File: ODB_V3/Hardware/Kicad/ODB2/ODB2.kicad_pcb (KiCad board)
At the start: 4 copper layers, 63.5 x 127 mm, 238 parts, among them IC1 W25Q512JVEIQ, J1 1715310000, J10 GPS_Conn_02x04_Top_Bottom, J15 Vin_XT30PW-F, J2 RFD_GT17HN-4DP-2HA56, J3 SYS_SW_Conn_01x05_Header, J5 MEM2067, J6 IdeFIX_GT17HN-4DP-2HA56, J7 1715250000, J8 1715310000, J9 1715250000, U1 STM32F412ZGTx, U10 ADXL382-2BCCZ-RL7, U11 SI5442DU-T1-GE3, U12 SI5442DU-T1-GE3, U13 L6981N33DR, U2 LM339, U3 SI5442DU-T1-GE3, U4 MS580301BA01-00, U6 BNO055, U7 MPQ9843GLE-5-AEC1-Z, U8 SI5442DU-T1-GE3, U9 MAX6612MXK, Y1 ABM8G-25.000MHZ-18-D2Y-T

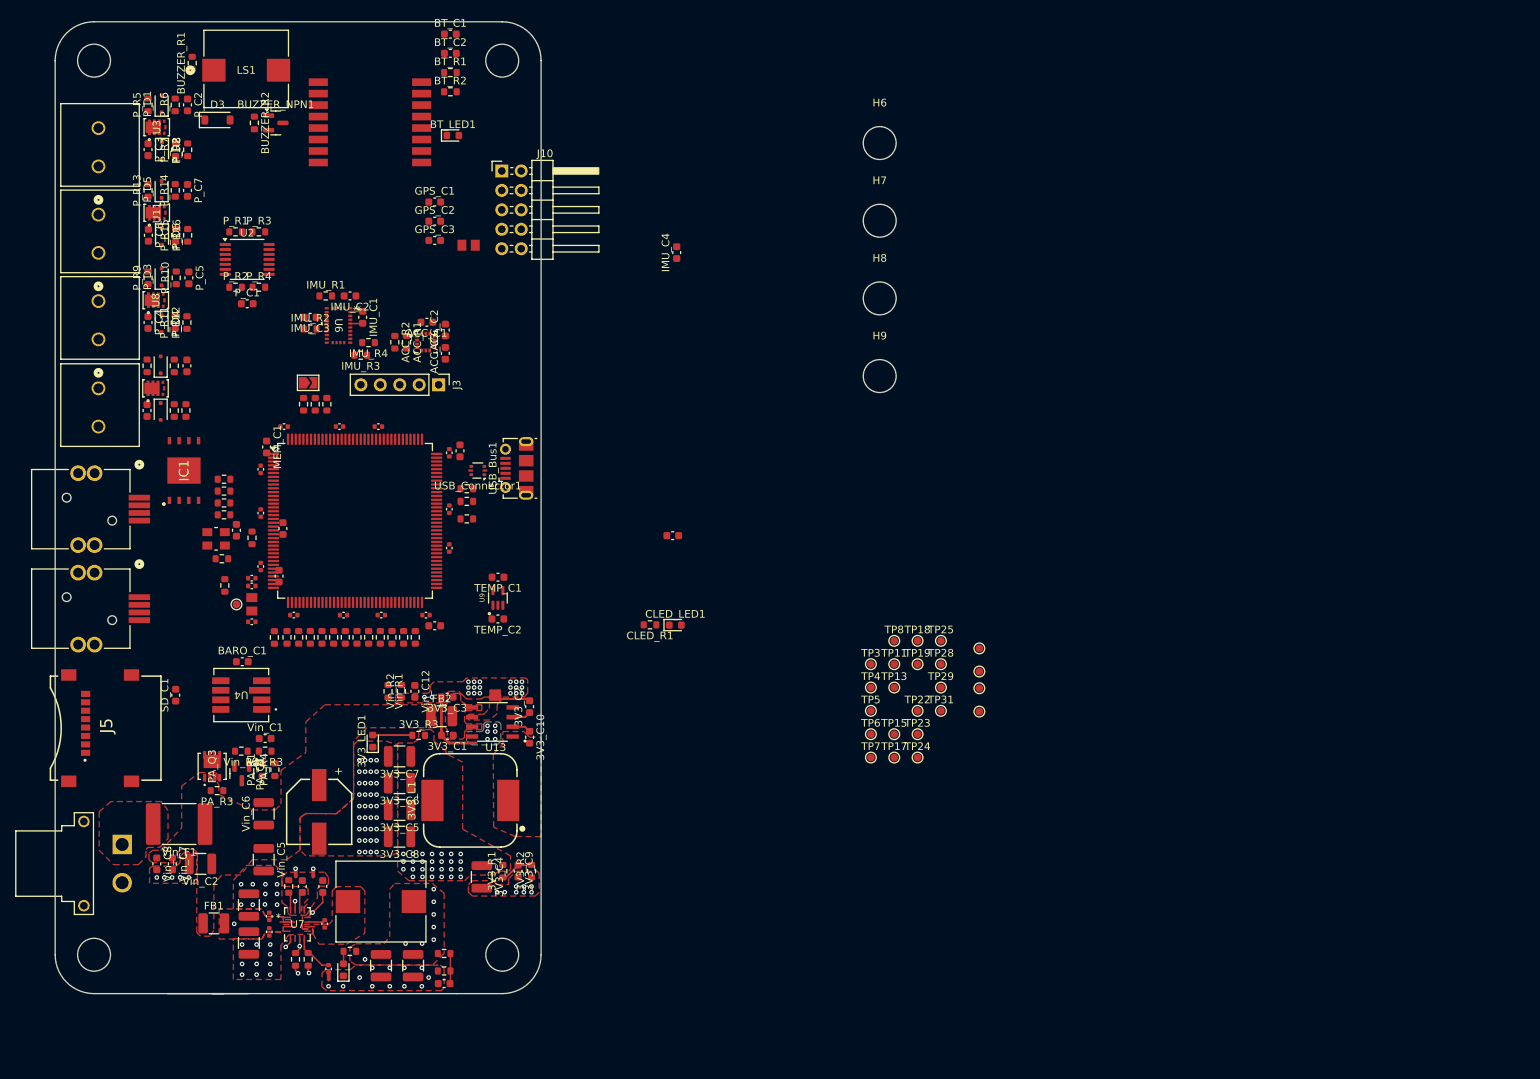
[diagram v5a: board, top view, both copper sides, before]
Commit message: WIP : finition layout, fix connecteur GPS, passage 4 couches -> 6 couches
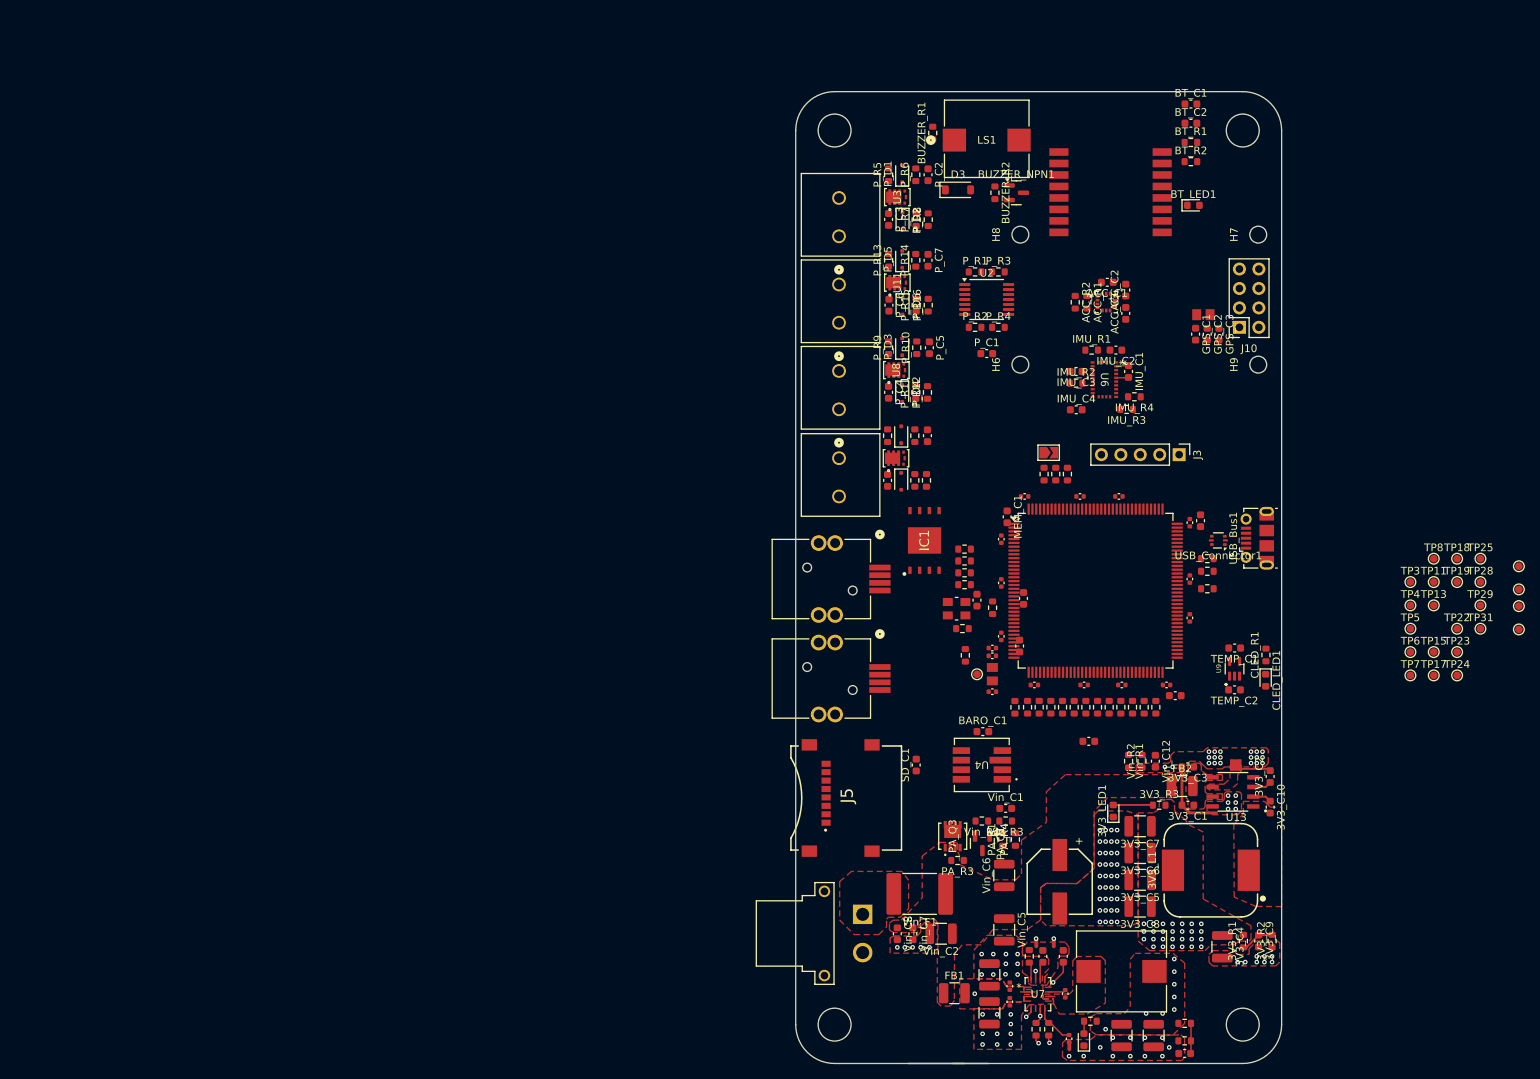
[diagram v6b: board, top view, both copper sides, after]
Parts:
- H6, H7, H8, H9: footprint MountingHole:MountingHole_4.3mm_M4 -> MountingHole:MountingHole_2.2mm_M2
- J10: footprint Connector_PinHeader_2.54mm:PinHeader_2x05_P2.54mm_Horizontal -> Connector_PinSocket_2.54mm:PinSocket_2x04_P2.54mm_Vertical
- moved GPS_C3 103.2 mm to (172.3, 60.8), turned to -90 degrees
- moved GPS_C2 102.0 mm to (170.8, 60.8), turned to -90 degrees
- moved GPS_C1 100.9 mm to (169.3, 60.8), turned to -90 degrees
- moved IMU_C1 100.3 mm to (160.5, 65.7)
- moved IMU_R1 100.3 mm to (155.7, 62.9)
- moved IMU_R4 100.3 mm to (161.3, 69.0)
- moved IMU_C3 100.3 mm to (153.7, 65.7)
- moved IMU_R2 100.3 mm to (153.7, 67.2)
- moved U6 100.3 mm to (157.4, 66.8)
- moved IMU_C2 100.3 mm to (158.9, 62.9)
- moved IMU_R3 100.3 mm to (160.3, 70.7)
- moved J10 98.5 mm to (175.0, 59.9), turned to 180 degrees
- moved Vin_C5 97.2 mm to (144.3, 138.7)
- moved 5V_C5 97.2 mm to (159.6, 152.5)
- moved BT_C1 97.2 mm to (168.7, 30.8)
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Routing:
- added copper zone on In3.Cu, net 5V_Main
- added copper zone on In4.Cu, net GND
- removed copper zone on In2.Cu, net 5V_Main
- removed copper zone on B.Cu, net GND
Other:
- copper layers 4 -> 6

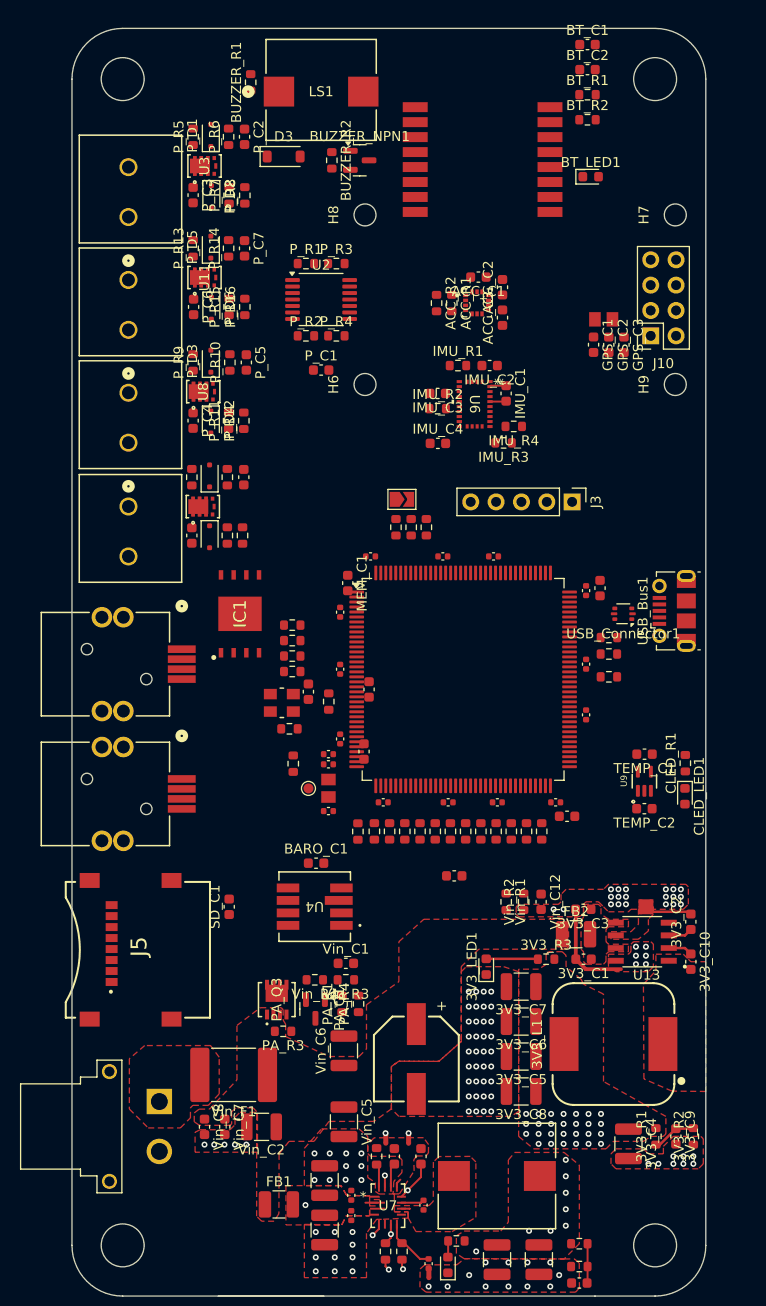
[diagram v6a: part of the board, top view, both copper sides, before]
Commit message: WIP : SD card under PCB, make board shorter in y axis
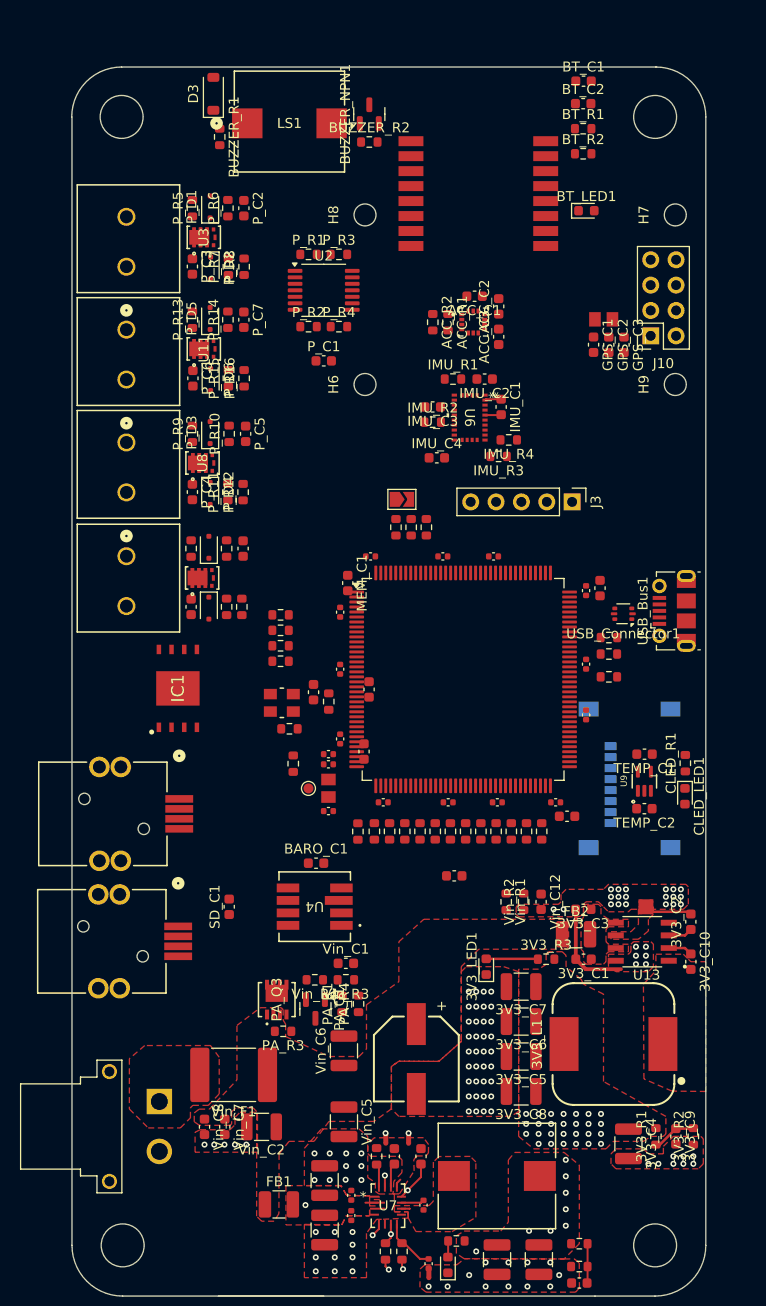
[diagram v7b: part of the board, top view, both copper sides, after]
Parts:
- J5: moved to B.Cu
- moved J5 52.9 mm to (173.6, 104.3), turned to 90 degrees
- moved J2 15.0 mm to (120.1, 107.8)
- moved J6 14.8 mm to (120.0, 120.6)
- moved IC1 9.72 mm to (127.6, 95.2)
- moved D3 9.43 mm to (131.2, 35.7), turned to 90 degrees
- moved P_D3 7.15 mm to (130.9, 69.6)
- moved P_D6 7.15 mm to (130.9, 64.3)
- moved P_C2 7.15 mm to (134.2, 47.1)
- moved P_C7 7.15 mm to (134.2, 58.3)
- moved P_C9 7.15 mm to (134.2, 81.2)
- moved P_D4 7.15 mm to (130.9, 75.7)
- moved P_D5 7.15 mm to (130.9, 58.2)
- moved P_D7 7.15 mm to (130.7, 81.1)
- moved P_D8 7.15 mm to (130.7, 87.2)
- moved P_R10 7.15 mm to (132.8, 69.7)
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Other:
- board size 63.5 x 127 mm -> 63.5 x 123.1 mm

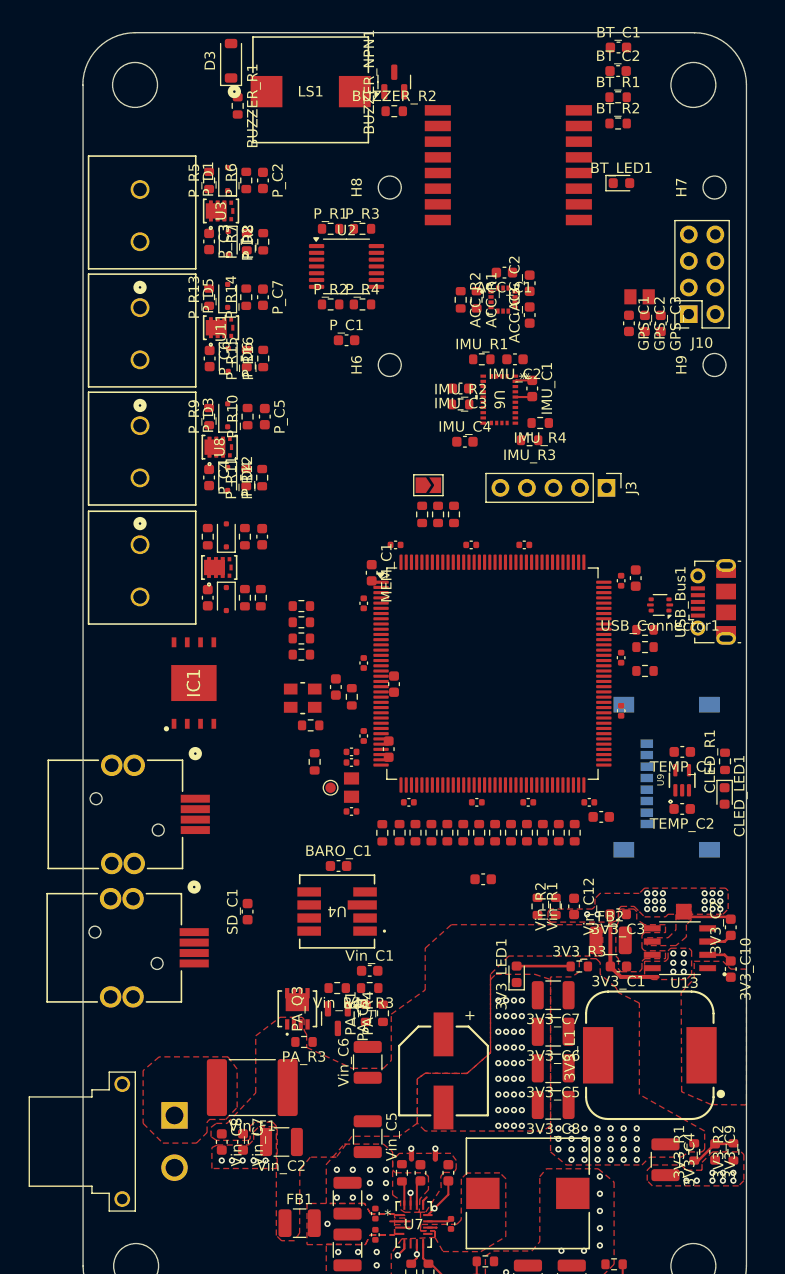
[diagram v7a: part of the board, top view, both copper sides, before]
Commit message: fix : modèles 3D pour connecteurs, changer capteur temp de place
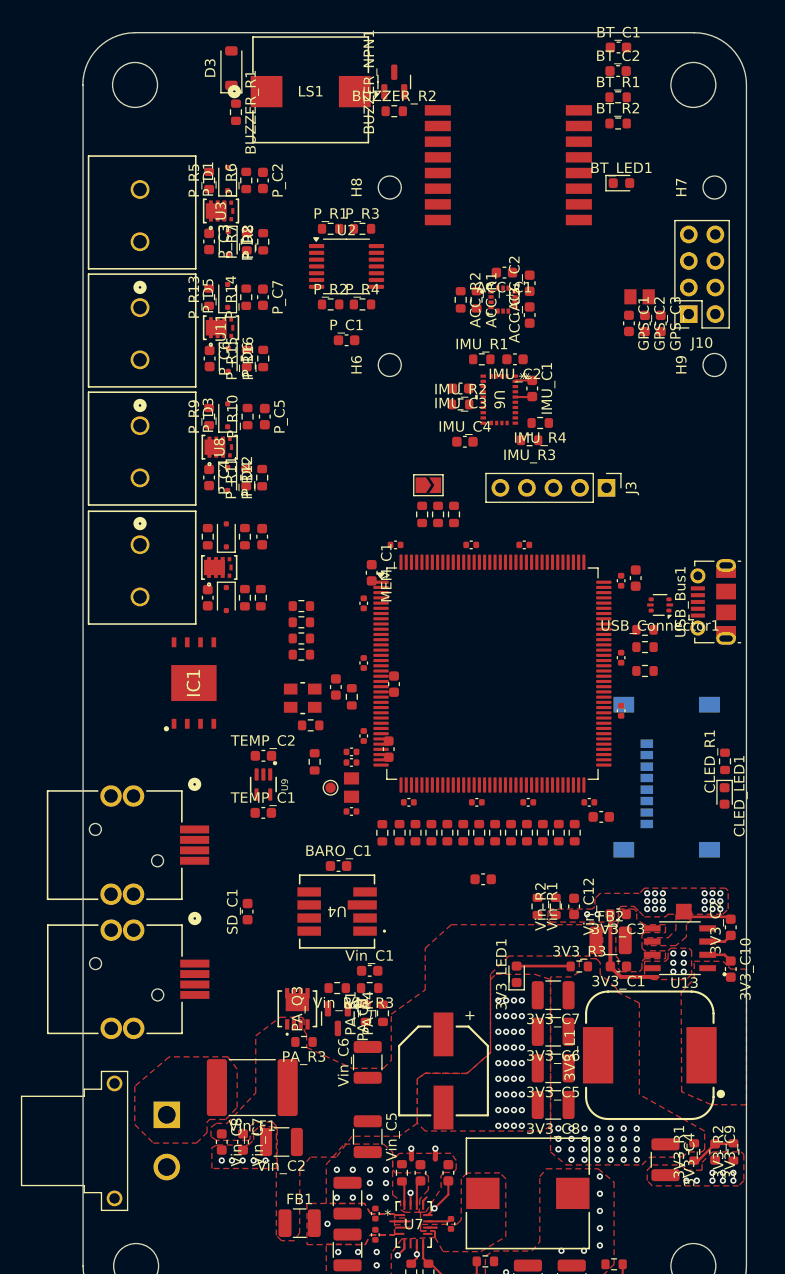
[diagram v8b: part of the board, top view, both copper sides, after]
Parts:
- moved TEMP_C1 40.5 mm to (134.3, 107.7), turned to 0 degrees
- moved TEMP_C2 40.4 mm to (134.3, 102.2), turned to 0 degrees
- moved U9 40.1 mm to (134.3, 105.0), turned to -90 degrees
- moved J2 15.8 mm to (120.1, 123.6)
- moved J6 9.83 mm to (120.1, 110.8)
- moved J15 0.74 mm to (120.0, 139.1)
- moved D3 0.71 mm to (131.2, 36.4)
- moved BUZZER_R1 0.63 mm to (131.7, 40.6)
